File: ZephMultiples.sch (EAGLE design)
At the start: 15 parts

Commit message: Power on the multiples board
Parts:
- added U$16: POWER, EurorackModularParts:POWER
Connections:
- new net GND: U$16.GND
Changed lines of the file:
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@@
 <layer number="48" name="Document" color="7" fill="1" visible="no" active="no"/>
 <layer number="49" name="Reference" color="7" fill="1" visible="no" active="no"/>
+<layer number="50" name="dxf" color="7" fill="1" visible="no" active="no"/>
 <layer number="51" name="tDocu" color="7" fill="1" visible="no" active="no"/>
 <layer number="52" name="bDocu" color="7" fill="1" visible="no" active="no"/>
+<layer number="53" name="tGND_GNDA" color="7" fill="9" visible="no" active="no"/>
+<layer number="54" name="bGND_GNDA" color="1" fill="9" visible="no" active="no"/>
+<layer number="56" name="wert" color="7" fill="1" visible="no" active="no"/>
 <layer number="91" name="Nets" color="2" fill="1" visible="yes" active="yes"/>
 <layer number="92" name="Busses" color="1" fill="1" visible="yes" active="yes"/>
@@
 <layer number="97" name="Info" color="7" fill="1" visible="yes" active="yes"/>
 <layer number="98" name="Guide" color="6" fill="1" visible="yes" active="yes"/>
+<layer number="100" name="Muster" color="7" fill="1" visible="no" active="no"/>
+<layer number="101" name="Patch_Top" color="12" fill="4" visible="yes" active="yes"/>
+<layer number="102" name="Vscore" color="7" fill="1" visible="yes" active="yes"/>
+<layer number="103" name="tMap" color="7" fill="1" visible="yes" active="yes"/>
+<layer number="104" name="Name" color="16" fill="1" visible="yes" active="yes"/>
+<layer number="105" name="tPlate" color="7" fill="1" visible="yes" active="yes"/>
+<layer number="106" name="bPlate" color="7" fill="1" visible="yes" active="yes"/>
+<layer number="107" name="Crop" color="7" fill="1" visible="yes" active="yes"/>
+<layer number="116" name="Patch_BOT" color="9" fill="4" visible="yes" active="yes"/>
+<layer number="121" name="_tsilk" color="7" fill="1" visible="yes" active="yes"/>
+<layer number="122" name="_bsilk" color="7" fill="1" visible="yes" active="yes"/>
+<layer number="125" name="_tNames" color="7" fill="1" visible="yes" active="yes"/>
+<layer number="144" name="Drill_legend" color="7" fill="1" visible="yes" active="yes"/>
+<layer number="151" name="HeatSink" color="7" fill="1" visible="yes" active="yes"/>
+<layer number="199" name="Contour" color="7" fill="1" visible="no" active="yes"/>
+<layer number="200" name="200bmp" color="1" fill="10" visible="yes" active="yes"/>
+<layer number="201" name="201bmp" color="2" fill="10" visible="yes" active="yes"/>
+<layer number="202" name="202bmp" color="3" fill="10" visible="yes" active="yes"/>
+<layer number="203" name="203bmp" color="4" fill="10" visible="yes" active="yes"/>
+<layer number="204" name="204bmp" color="5" fill="10" visible="yes" active="yes"/>
+<layer number="205" name="205bmp" color="6" fill="10" visible="yes" active="yes"/>
+<layer number="206" name="206bmp" color="7" fill="10" visible="yes" active="yes"/>
+<layer number="207" name="207bmp" color="8" fill="10" visible="yes" active="yes"/>
+<layer number="208" name="208bmp" color="9" fill="10" visible="yes" active="yes"/>
+<layer number="209" name="209bmp" color="7" fill="1" visible="yes" active="yes"/>
+<layer number="210" name="210bmp" color="7" fill="1" visible="yes" active="yes"/>
+<layer number="211" name="211bmp" color="7" fill="1" visible="yes" active="yes"/>
+<layer number="212" name="212bmp" color="7" fill="1" visible="yes" active="yes"/>
+<layer number="213" name="213bmp" color="7" fill="1" visible="yes" active="yes"/>
+<layer number="214" name="214bmp" color="7" fill="1" visible="yes" active="yes"/>
+<layer number="215" name="215bmp" color="7" fill="1" visible="yes" active="yes"/>
+<layer number="216" name="216bmp" color="7" fill="1" visible="yes" active="yes"/>
+<layer number="217" name="217bmp" color="18" fill="1" visible="no" active="no"/>
+<layer number="218" name="218bmp" color="19" fill="1" visible="no" active="no"/>
+<layer number="219" name="219bmp" color="20" fill="1" visible="no" active="no"/>
+<layer number="220" name="220bmp" color="21" fill="1" visible="no" active="no"/>
+<layer number="221" name="221bmp" color="22" fill="1" visible="no" active="no"/>
+<layer number="222" name="222bmp" color="23" fill="1" visible="no" active="no"/>
+<layer number="223" name="223bmp" color="24" fill="1" visible="no" active="no"/>
+<layer number="224" name="224bmp" color="25" fill="1" visible="no" active="no"/>
+<layer number="250" name="Descript" color="3" fill="1" visible="no" active="no"/>
+<layer number="251" name="SMDround" color="12" fill="11" visible="no" active="no"/>
+<layer number="254" name="cooling" color="7" fill="1" visible="yes" active="yes"/>
 </layers>
 <schematic xreflabel="%F%N/%S.%C%R" xrefpart="/%S.%C%R">
@@
 <part name="U$14" library="erthenvar" deviceset="AUDIO-JACK" device="ERTHENVAR"/>
 <part name="U$15" library="EurorackModularParts" deviceset="EURORACK_PANEL" device="8HPPCB"/>
+<part name="U$16" library="EurorackModularParts" deviceset="POWER" device=""/>
+<part name="GND1" library="SparkFun-Aesthetics" deviceset="GND" device=""/>
 </parts>
 <sheets>
@@
 <instance part="U$14" gate="G$1" x="22.86" y="-27.94"/>
 <instance part="U$15" gate="G$1" x="119.38" y="50.8"/>
+<instance part="U$16" gate="G$1" x="124.46" y="88.9"/>
+<instance part="GND1" gate="1" x="137.16" y="91.44" rot="R90"/>
 </instances>
 <busses>
@@
 </segment>
 </net>
+<net name="GND" class="0">
+<segment>
+<pinref part="U$16" gate="G$1" pin="GND"/>
+<pinref part="GND1" gate="1" pin="GND"/>
+</segment>
+</net>

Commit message: Goldfish Frontpanel Progress + eurolib extensions
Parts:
- added U$17: AUDIO-JACKINPUT, EurorackModularParts:AUDIO-JACKINPUT
- added U$18, U$19, U$20, U$21, U$22, U$23: AUDIO-JACKOUTPUT, EurorackModularParts:AUDIO-JACKOUTPUT
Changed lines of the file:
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@@
 <part name="U$16" library="EurorackModularParts" deviceset="POWER" device=""/>
 <part name="GND1" library="SparkFun-Aesthetics" deviceset="GND" device=""/>
+<part name="U$17" library="EurorackModularParts" deviceset="AUDIO-JACK" device="INPUT"/>
+<part name="U$18" library="EurorackModularParts" deviceset="AUDIO-JACK" device="OUTPUT"/>
+<part name="U$19" library="EurorackModularParts" deviceset="AUDIO-JACK" device="OUTPUT"/>
+<part name="U$20" library="EurorackModularParts" deviceset="AUDIO-JACK" device="OUTPUT"/>
+<part name="U$21" library="EurorackModularParts" deviceset="AUDIO-JACK" device="OUTPUT"/>
+<part name="U$22" library="EurorackModularParts" deviceset="AUDIO-JACK" device="OUTPUT"/>
+<part name="U$23" library="EurorackModularParts" deviceset="AUDIO-JACK" device="OUTPUT"/>
 </parts>
 <sheets>
@@
 <instance part="U$16" gate="G$1" x="124.46" y="88.9"/>
 <instance part="GND1" gate="1" x="137.16" y="91.44" rot="R90"/>
+<instance part="U$17" gate="G$1" x="213.36" y="66.04"/>
+<instance part="U$18" gate="G$1" x="276.86" y="101.6"/>
+<instance part="U$19" gate="G$1" x="276.86" y="78.74"/>
+<instance part="U$20" gate="G$1" x="276.86" y="55.88"/>
+<instance part="U$21" gate="G$1" x="276.86" y="33.02"/>
+<instance part="U$22" gate="G$1" x="276.86" y="10.16"/>
+<instance part="U$23" gate="G$1" x="276.86" y="-12.7"/>
 </instances>
 <busses>

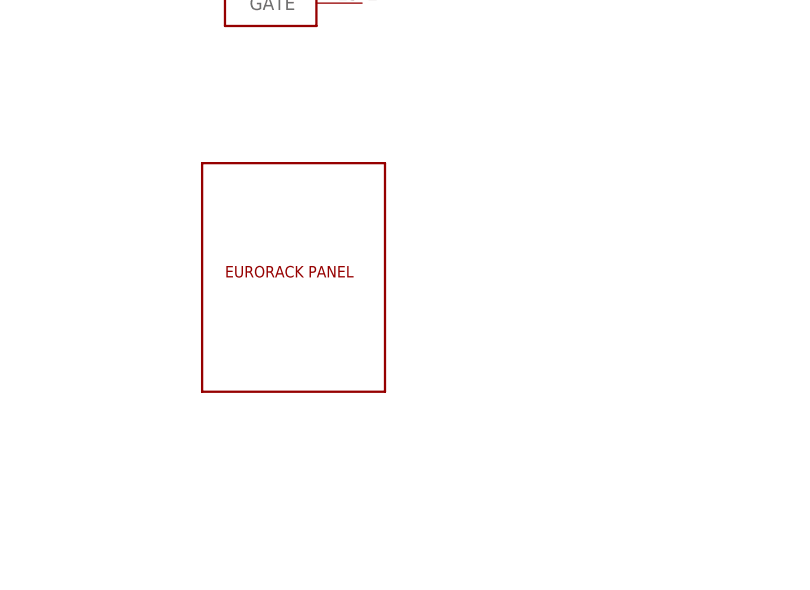
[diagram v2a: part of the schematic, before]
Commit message: Updated europarts library in all boards.
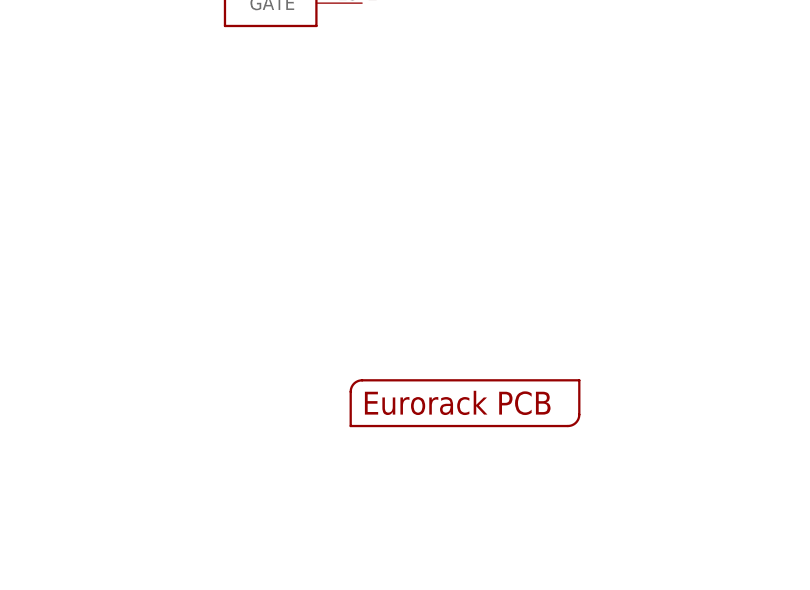
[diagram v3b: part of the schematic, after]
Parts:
- U$15: value EURORACK_PANEL8HPPCB -> EURORACK_PCB8HP; device EurorackModularParts:EURORACK_PANEL8HPPCB -> EurorackModularParts:EURORACK_PCB8HP
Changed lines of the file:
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@@
 <layer number="54" name="bGND_GNDA" color="1" fill="9" visible="no" active="no"/>
 <layer number="56" name="wert" color="7" fill="1" visible="no" active="no"/>
+<layer number="57" name="tCAD" color="7" fill="1" visible="no" active="no"/>
 <layer number="91" name="Nets" color="2" fill="1" visible="yes" active="yes"/>
 <layer number="92" name="Busses" color="1" fill="1" visible="yes" active="yes"/>
@@
 <layer number="106" name="bPlate" color="7" fill="1" visible="yes" active="yes"/>
 <layer number="107" name="Crop" color="7" fill="1" visible="yes" active="yes"/>
+<layer number="108" name="fp8" color="7" fill="1" visible="yes" active="yes"/>
+<layer number="109" name="fp9" color="7" fill="1" visible="yes" active="yes"/>
+<layer number="110" name="110" color="7" fill="1" visible="yes" active="yes"/>
+<layer number="111" name="111" color="7" fill="1" visible="yes" active="yes"/>
+<layer number="112" name="tSilk" color="7" fill="1" visible="yes" active="yes"/>
 <layer number="116" name="Patch_BOT" color="9" fill="4" visible="yes" active="yes"/>
+<layer number="118" name="Rect_Pads" color="7" fill="1" visible="yes" active="yes"/>
 <layer number="121" name="_tsilk" color="7" fill="1" visible="yes" active="yes"/>
 <layer number="122" name="_bsilk" color="7" fill="1" visible="yes" active="yes"/>
+<layer number="123" name="tTestmark" color="7" fill="1" visible="yes" active="yes"/>
+<layer number="124" name="bTestmark" color="7" fill="1" visible="yes" active="yes"/>
 <layer number="125" name="_tNames" color="7" fill="1" visible="yes" active="yes"/>
+<layer number="126" name="_bNames" color="7" fill="1" visible="yes" active="yes"/>
+<layer number="127" name="_tValues" color="7" fill="1" visible="yes" active="yes"/>
+<layer number="128" name="_bValues" color="7" fill="1" visible="yes" active="yes"/>
+<layer number="131" name="tAdjust" color="7" fill="1" visible="yes" active="yes"/>
+<layer number="132" name="bAdjust" color="7" fill="1" visible="yes" active="yes"/>
+<layer number="133" name="Ports" color="7" fill="1" visible="yes" active="yes"/>
+<layer number="134" name="Port2" color="7" fill="1" visible="yes" active="yes"/>
+<layer number="135" name="Port3" color="7" fill="1" visible="yes" active="yes"/>
 <layer number="144" name="Drill_legend" color="7" fill="1" visible="yes" active="yes"/>
+<layer number="150" name="Notes" color="7" fill="1" visible="yes" active="yes"/>
 <layer number="151" name="HeatSink" color="7" fill="1" visible="yes" active="yes"/>
+<layer number="152" name="_bDocu" color="7" fill="1" visible="yes" active="yes"/>
+<layer number="153" name="FabDoc1" color="7" fill="1" visible="yes" active="yes"/>
+<layer number="154" name="FabDoc2" color="7" fill="1" visible="yes" active="yes"/>
+<layer number="155" name="FabDoc3" color="7" fill="1" visible="yes" active="yes"/>
 <layer number="199" name="Contour" color="7" fill="1" visible="no" active="yes"/>
 <layer number="200" name="200bmp" color="1" fill="10" visible="yes" active="yes"/>
@@
 <layer number="223" name="223bmp" color="24" fill="1" visible="no" active="no"/>
 <layer number="224" name="224bmp" color="25" fill="1" visible="no" active="no"/>
+<layer number="226" name="topsilk" color="7" fill="1" visible="yes" active="yes"/>
+<layer number="231" name="Eagle3D_PG1" color="7" fill="1" visible="yes" active="yes"/>
+<layer number="232" name="Eagle3D_PG2" color="7" fill="1" visible="yes" active="yes"/>
+<layer number="233" name="Eagle3D_PG3" color="7" fill="1" visible="yes" active="yes"/>
+<layer number="248" name="Housing" color="7" fill="1" visible="yes" active="yes"/>
+<layer number="249" name="Edge" color="7" fill="1" visible="yes" active="yes"/>
 <layer number="250" name="Descript" color="3" fill="1" visible="no" active="no"/>
 <layer number="251" name="SMDround" color="12" fill="11" visible="no" active="no"/>
@@
 <part name="U$13" library="erthenvar" deviceset="AUDIO-JACK" device="ERTHENVAR"/>
 <part name="U$14" library="erthenvar" deviceset="AUDIO-JACK" device="ERTHENVAR"/>
-<part name="U$15" library="EurorackModularParts" deviceset="EURORACK_PANEL" device="8HPPCB"/>
 <part name="U$16" library="EurorackModularParts" deviceset="POWER" device=""/>
 <part name="GND1" library="SparkFun-Aesthetics" deviceset="GND" device=""/>
@@
 <part name="U$22" library="EurorackModularParts" deviceset="AUDIO-JACK" device="OUTPUT"/>
 <part name="U$23" library="EurorackModularParts" deviceset="AUDIO-JACK" device="OUTPUT"/>
+<part name="U$15" library="EurorackModularParts" deviceset="EURORACK_PCB" device="8HP"/>
 </parts>
 <sheets>
@@
 <instance part="U$13" gate="G$1" x="66.04" y="-10.16"/>
 <instance part="U$14" gate="G$1" x="22.86" y="-27.94"/>
-<instance part="U$15" gate="G$1" x="119.38" y="50.8"/>
 <instance part="U$16" gate="G$1" x="124.46" y="88.9"/>
 <instance part="GND1" gate="1" x="137.16" y="91.44" rot="R90"/>
@@
 <instance part="U$22" gate="G$1" x="276.86" y="10.16"/>
 <instance part="U$23" gate="G$1" x="276.86" y="-12.7"/>
+<instance part="U$15" gate="G$1" x="134.62" y="35.56"/>
 </instances>
 <busses>
